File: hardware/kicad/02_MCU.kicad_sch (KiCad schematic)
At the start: 17 parts, among them SW1 RESET, SW2 BOOT, U3 ESP32-S3-MINI-1-N8

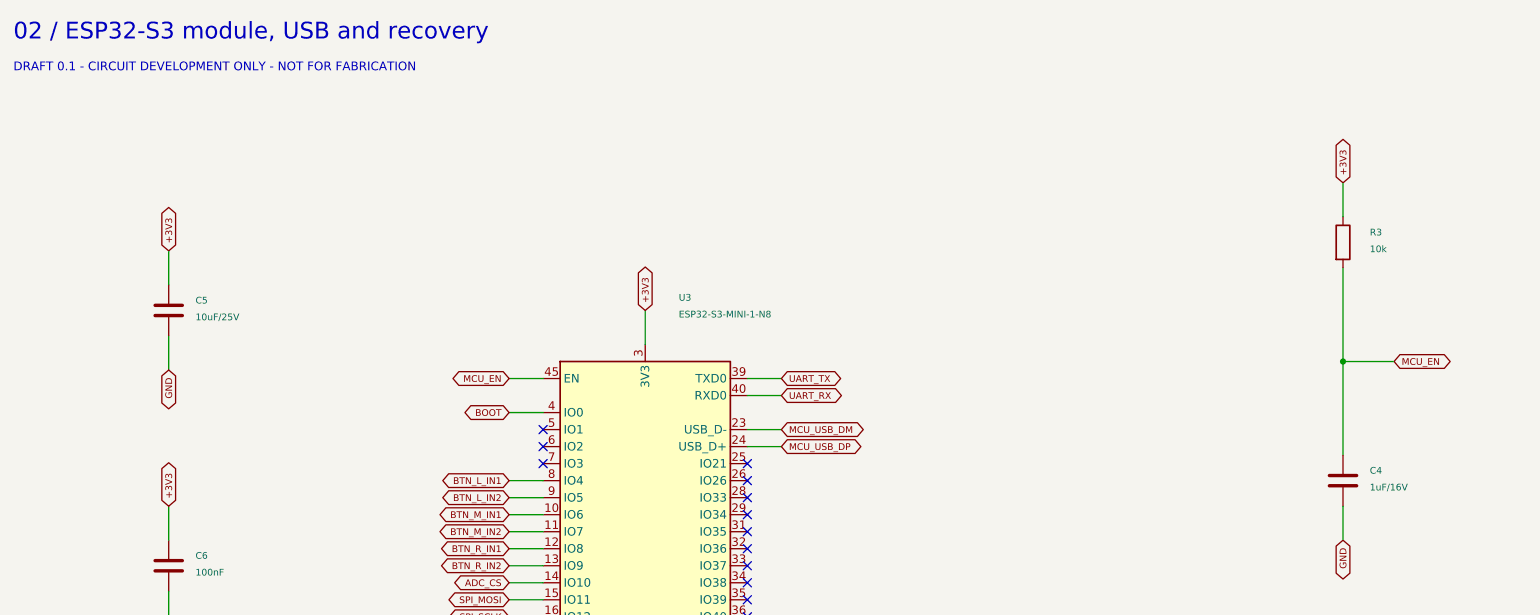
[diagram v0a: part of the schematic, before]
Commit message: Resolve KiCad component sourcing and missing footprints
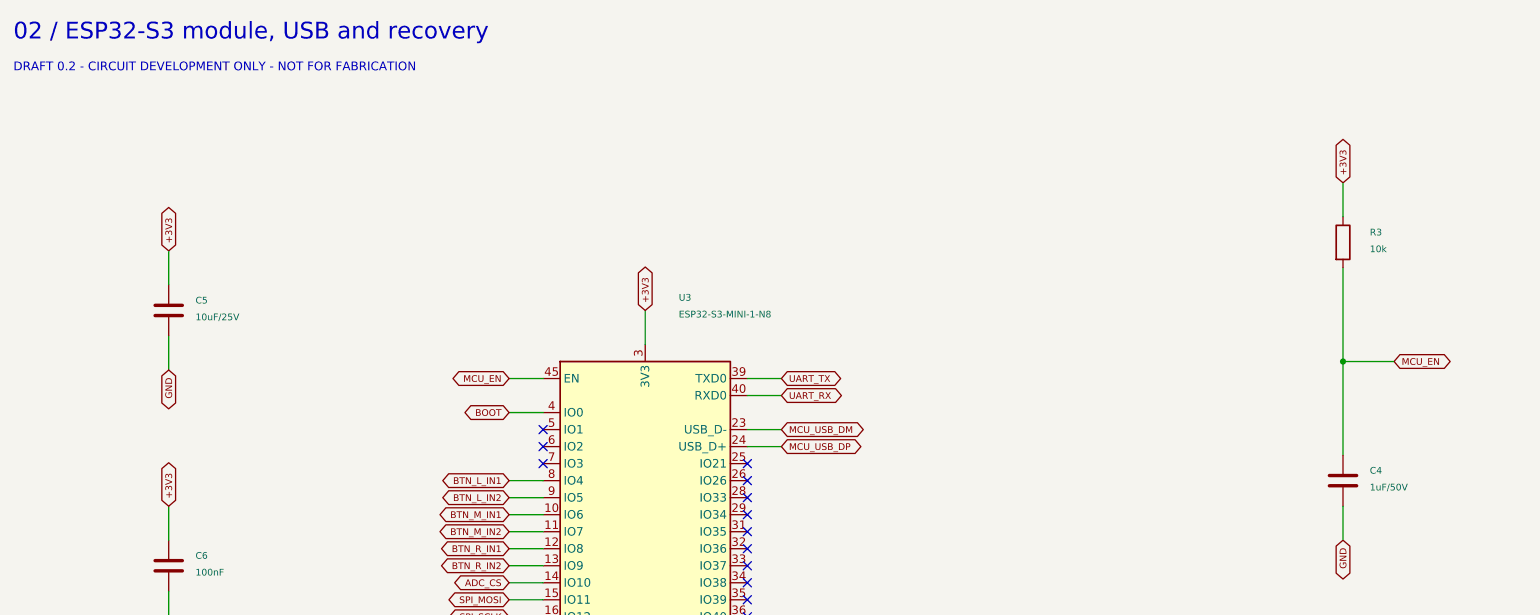
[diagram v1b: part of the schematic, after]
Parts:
- C4: value 1uF/16V -> 1uF/50V; Checked (none) -> 2026-09-08; JLCPCB Library Type (none) -> Basic; JLCPCB Part # (none) -> C15849; LCSC (none) -> C15849; MPN (none) -> CL10A105KB8NNNC; Manufacturer (none) -> Samsung Electro-Mechanics; Sourcing Status TBD - not orderable -> JLCPCB catalog verified; stock/quote refresh required; Supplier URL (none) -> https://jlcpcb.com/partdetail/16531-CL10A105KB8NNNC/C15849
- SW1, SW2: footprint (none) -> Button_Switch_SMD:SW_SPST_TS-1088-xR020; Checked (none) -> 2026-09-08; JLCPCB Library Type (none) -> Basic; JLCPCB Part # (none) -> C720477; LCSC (none) -> C720477; MPN (none) -> TS-1088-AR02016; Manufacturer (none) -> XUNPU; Sourcing Status TBD - select JLC tactile switch and footprint -> JLCPCB catalog verified; stock/quote refresh required; Supplier URL (none) -> https://jlcpcb.com/partdetail/XUNPU-TS_1088AR02016/C720477
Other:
- note added: "DRAFT 0.2 - CIRCUIT DEVELOPMENT ONLY - NOT FOR FABRICATION"
- note removed: "DRAFT 0.1 - CIRCUIT DEVELOPMENT ONLY - NOT FOR FABRICATION"
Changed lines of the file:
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@@
     (title "MagMouse - 02_MCU")
     (date "2026-09-08")
-    (rev "0.1 DRAFT")
+    (rev "0.2 DRAFT")
     (company "MagMouse")
     (comment 1 "NOT FOR FABRICATION - unresolved circuits listed in README.md"))
@@
       (justify left top))
 )
-  (text "DRAFT 0.1 - CIRCUIT DEVELOPMENT ONLY - NOT FOR FABRICATION"
+  (text "DRAFT 0.2 - CIRCUIT DEVELOPMENT ONLY - NOT FOR FABRICATION"
     (at 20 24 0)
     (effects
@@
           (size 1.0 1.0))
         (justify left)))
-    (property "Value" "1uF/16V"
+    (property "Value" "1uF/50V"
       (at 222.44 87.36 0)
       (effects
@@
           (size 1.0 1.0))
         (justify left)))
-    (property "Manufacturer" ""
+    (property "Manufacturer" "Samsung Electro-Mechanics"
       (at 218.44 86.36 0)
       (hide yes)
@@
           (size 1.0 1.0))
         (justify left)))
-    (property "MPN" ""
+    (property "MPN" "CL10A105KB8NNNC"
       (at 218.44 86.36 0)
       (hide yes)
@@
           (size 1.0 1.0))
         (justify left)))
-    (property "LCSC" ""
+    (property "LCSC" "C15849"
       (at 218.44 86.36 0)
       (hide yes)
@@
           (size 1.0 1.0))
         (justify left)))
-    (property "JLCPCB Part #" ""
+    (property "JLCPCB Part #" "C15849"
       (at 218.44 86.36 0)
       (hide yes)
@@
           (size 1.0 1.0))
         (justify left)))
-    (property "Sourcing Status" "TBD - not orderable"
+    (property "Sourcing Status" "JLCPCB catalog verified; stock/quote refresh required"
       (at 218.44 86.36 0)
       (hide yes)
@@
           (size 1.0 1.0))
         (justify left)))
-    (property "Checked" ""
+    (property "Checked" "2026-09-08"
       (at 218.44 86.36 0)
       (hide yes)
@@
         (path "/5d73110b-42e6-5c5c-9841-c82d60f67640/d5629ffc-c70c-5a32-8660-d50043bd3c4c"
           (reference "C4")
-          (unit 1)))))
+          (unit 1))))
+    (property "Supplier URL" "https://jlcpcb.com/partdetail/16531-CL10A105KB8NNNC/C15849"
+      (at 218.44 86.36 0)
+      (hide yes)
+      (effects
+        (font
+          (size 1 1))
+        (justify left)))
+    (property "JLCPCB Library Type" "Basic"
+      (at 218.44 86.36 0)
+      (hide yes)
+      (effects
+        (font
+          (size 1 1))
+        (justify left))))
   (wire
     (pts
@@
           (size 1.0 1.0))
         (justify left)))
-    (property "Footprint" ""
+    (property "Footprint" "Button_Switch_SMD:SW_SPST_TS-1088-xR020"
       (at 218.44 121.92 0)
       (hide yes)
@@
           (size 1.0 1.0))
         (justify left)))
-    (property "Datasheet" ""
+    (property "Datasheet" "https://datasheet.lcsc.com/datasheet/pdf/0475ac02febf455ca9ddcfb380b0df0d.pdf?productCode=C720477"
       (at 218.44 121.92 0)
       (hide yes)
@@
           (size 1.0 1.0))
         (justify left)))
-    (property "Manufacturer" ""
+    (property "Manufacturer" "XUNPU"
       (at 218.44 121.92 0)
       (hide yes)
@@
           (size 1.0 1.0))
         (justify left)))
-    (property "MPN" ""
+    (property "MPN" "TS-1088-AR02016"
       (at 218.44 121.92 0)
       (hide yes)
@@
           (size 1.0 1.0))
         (justify left)))
-    (property "LCSC" ""
+    (property "LCSC" "C720477"
       (at 218.44 121.92 0)
       (hide yes)
@@
           (size 1.0 1.0))
         (justify left)))
-    (property "JLCPCB Part #" ""
+    (property "JLCPCB Part #" "C720477"
       (at 218.44 121.92 0)
       (hide yes)
@@
           (size 1.0 1.0))
         (justify left)))
-    (property "Sourcing Status" "TBD - select JLC tactile switch and footprint"
+    (property "Sourcing Status" "JLCPCB catalog verified; stock/quote refresh required"
       (at 218.44 121.92 0)
       (hide yes)
@@
           (size 1.0 1.0))
         (justify left)))
-    (property "Checked" ""
+    (property "Checked" "2026-09-08"
       (at 218.44 121.92 0)
       (hide yes)
@@
         (path "/5d73110b-42e6-5c5c-9841-c82d60f67640/d5629ffc-c70c-5a32-8660-d50043bd3c4c"
           (reference "SW1")
-          (unit 1)))))
+          (unit 1))))
+    (property "Supplier URL" "https://jlcpcb.com/partdetail/XUNPU-TS_1088AR02016/C720477"
+      (at 218.44 121.92 0)
+      (hide yes)
+      (effects
+        (font
+          (size 1 1))
+        (justify left)))
+    (property "JLCPCB Library Type" "Basic"
+      (at 218.44 121.92 0)
+      (hide yes)
+      (effects
+        (font
+          (size 1 1))
+        (justify left))))
   (wire
     (pts
@@
           (size 1.0 1.0))
         (justify left)))
-    (property "Footprint" ""
+    (property "Footprint" "Button_Switch_SMD:SW_SPST_TS-1088-xR020"
       (at 289.56 121.92 0)
       (hide yes)
@@
           (size 1.0 1.0))
         (justify left)))
-    (property "Datasheet" ""
+    (property "Datasheet" "https://datasheet.lcsc.com/datasheet/pdf/0475ac02febf455ca9ddcfb380b0df0d.pdf?productCode=C720477"
       (at 289.56 121.92 0)
       (hide yes)
@@
           (size 1.0 1.0))
         (justify left)))
-    (property "Manufacturer" ""
+    (property "Manufacturer" "XUNPU"
       (at 289.56 121.92 0)
       (hide yes)
@@
           (size 1.0 1.0))
         (justify left)))
-    (property "MPN" ""
+    (property "MPN" "TS-1088-AR02016"
       (at 289.56 121.92 0)
       (hide yes)
@@
           (size 1.0 1.0))
         (justify left)))
-    (property "LCSC" ""
+    (property "LCSC" "C720477"
       (at 289.56 121.92 0)
       (hide yes)
@@
           (size 1.0 1.0))
         (justify left)))
-    (property "JLCPCB Part #" ""
+    (property "JLCPCB Part #" "C720477"
       (at 289.56 121.92 0)
       (hide yes)
@@
           (size 1.0 1.0))
         (justify left)))
-    (property "Sourcing Status" "TBD - select JLC tactile switch and footprint"
+    (property "Sourcing Status" "JLCPCB catalog verified; stock/quote refresh required"
       (at 289.56 121.92 0)
       (hide yes)
@@
           (size 1.0 1.0))
         (justify left)))
-    (property "Checked" ""
+    (property "Checked" "2026-09-08"
       (at 289.56 121.92 0)
       (hide yes)
@@
         (path "/5d73110b-42e6-5c5c-9841-c82d60f67640/d5629ffc-c70c-5a32-8660-d50043bd3c4c"
           (reference "SW2")
-          (unit 1)))))
-  (wire
-    (pts
+          (unit 1))))
+    (property "Supplier URL" "https://jlcpcb.com/partdetail/XUNPU-TS_1088AR02016/C720477"
+      (at 289.56 121.92 0)
+      (hide yes)
+      (effects
+        (font
+          (size 1 1))
+        (justify left)))
+    (property "JLCPCB Library Type" "Basic"
+      (at 289.56 121.92 0)
+      (hide yes)
+      (effects
+        (font
+          (size 1 1))
+        (justify left))))
+  (wire
+    (pts

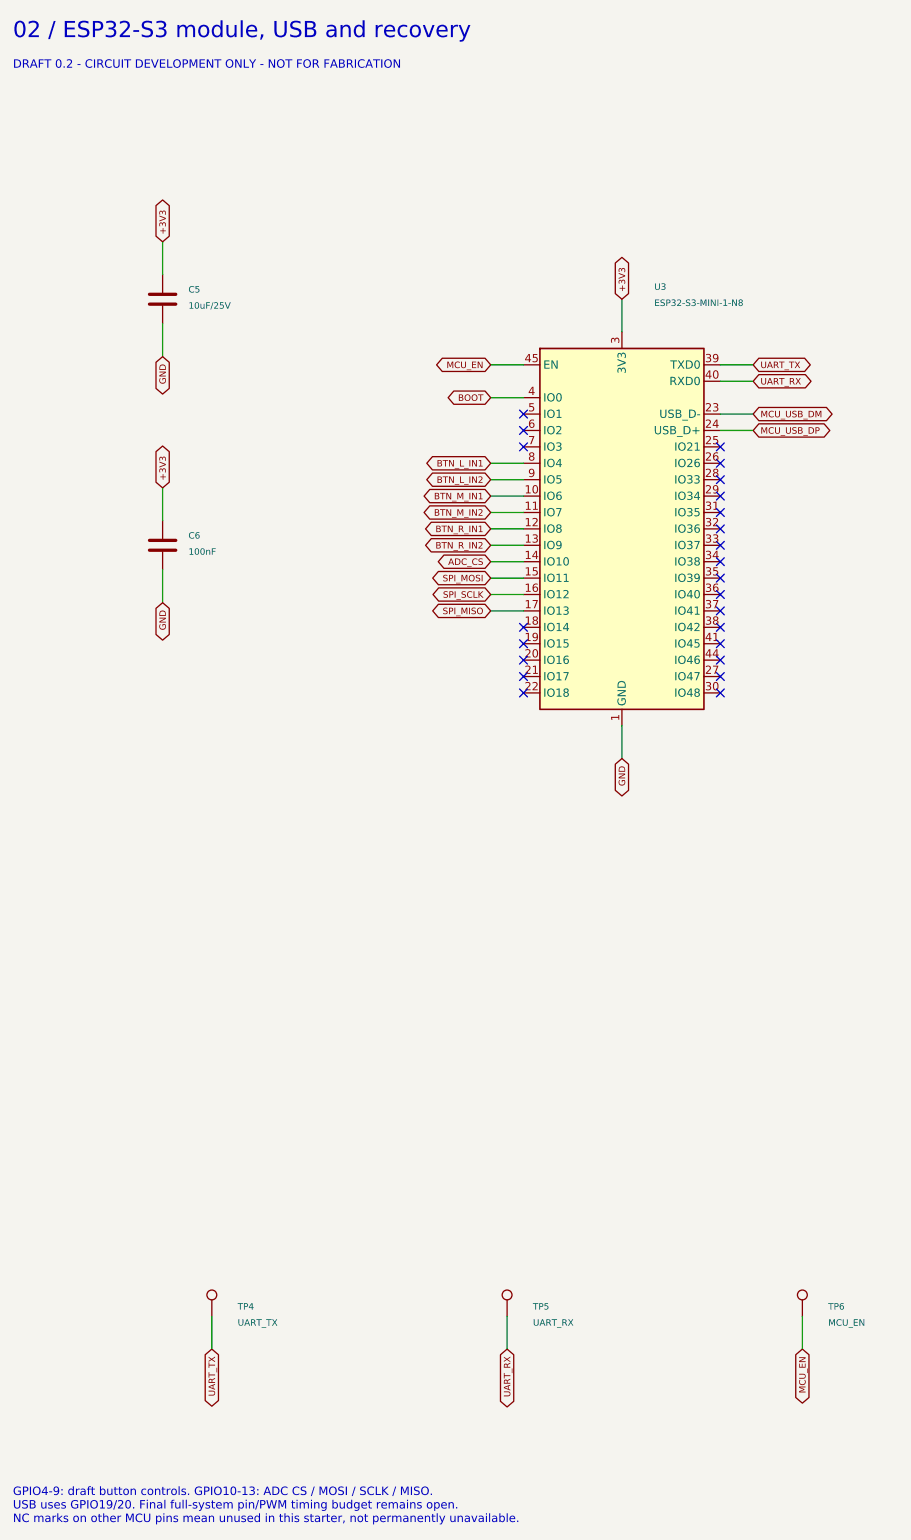
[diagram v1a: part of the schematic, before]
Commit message: Implement USB-C power control schematic and validation
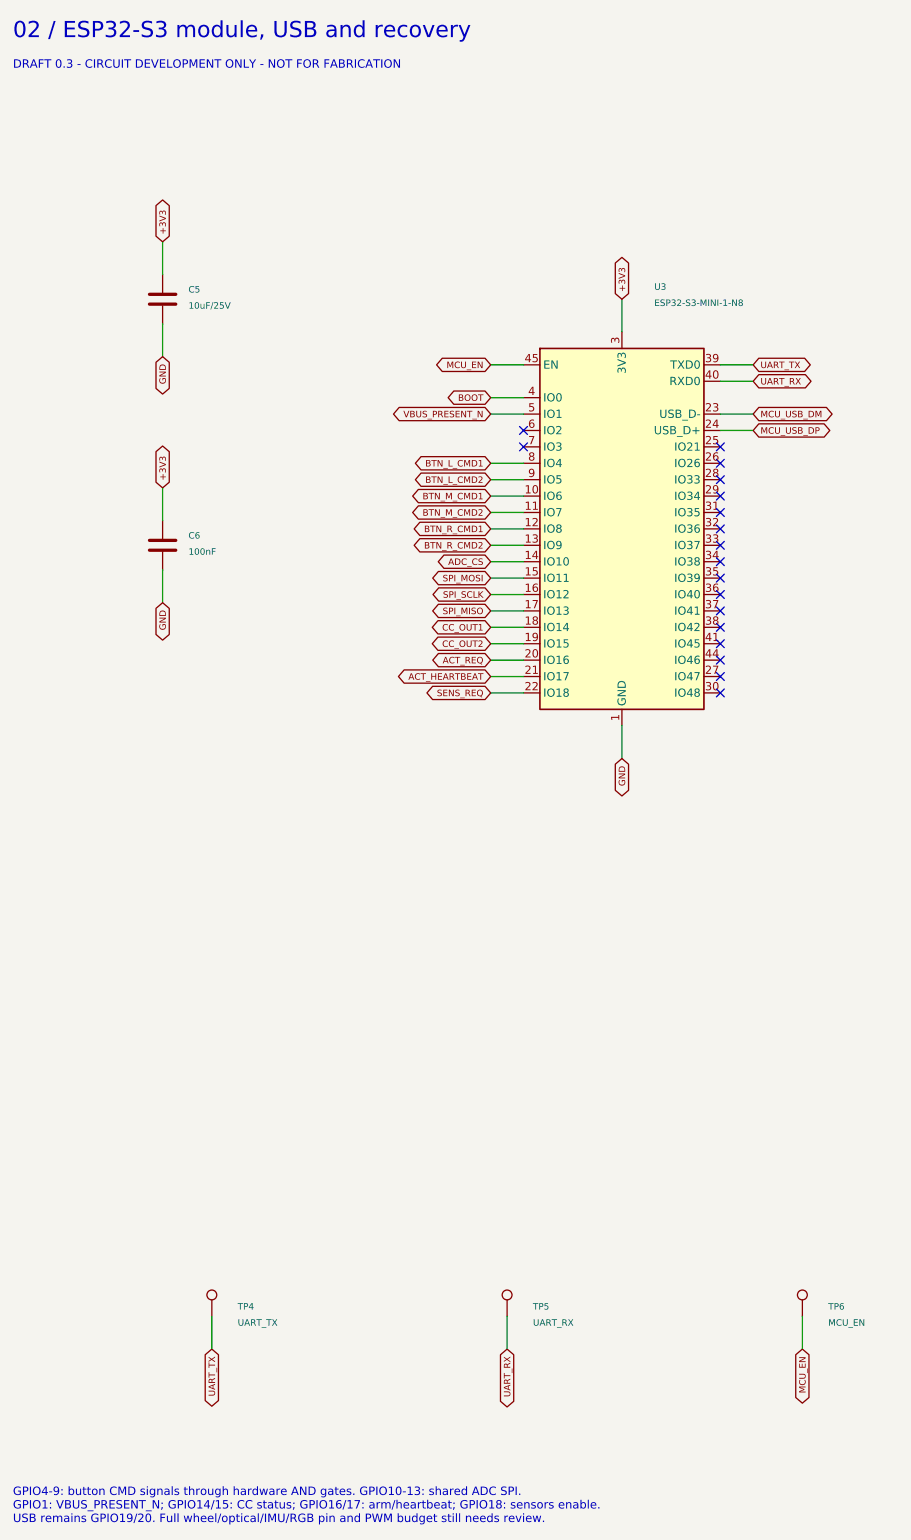
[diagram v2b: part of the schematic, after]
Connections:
- net CC_OUT1: now reaches U3.18 (IO14)
- net CC_OUT2: now reaches U3.19 (IO15)
- net ACT_REQ: now reaches U3.20 (IO16)
- net ACT_HEARTBEAT: now reaches U3.21 (IO17)
- net SENS_REQ: now reaches U3.22 (IO18)
- net VBUS_PRESENT_N: now reaches U3.5 (IO1)
- net BTN_L_IN1 renamed BTN_L_CMD1
- net BTN_L_IN2 renamed BTN_L_CMD2
- net BTN_M_IN1 renamed BTN_M_CMD1
- net BTN_M_IN2 renamed BTN_M_CMD2
- net BTN_R_IN1 renamed BTN_R_CMD1
- net BTN_R_IN2 renamed BTN_R_CMD2
- no-connect marks 24 -> 18
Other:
- note added: "DRAFT 0.3 - CIRCUIT DEVELOPMENT ONLY - NOT FOR FABRICATION"
- note added: "GPIO4-9: button CMD signals through hardware AND gates. GPIO10-13: shared ADC SPI. GPIO1: VBUS_PRESENT_N; GPIO14/15: CC status; GPIO16/17: arm/heartbeat; GPIO18: sensors enable. USB remains GPIO19/20. Full wheel/optical/IMU/RGB pin and PWM budget still needs review."
- note removed: "DRAFT 0.2 - CIRCUIT DEVELOPMENT ONLY - NOT FOR FABRICATION"
- note removed: "GPIO4-9: draft button controls. GPIO10-13: ADC CS / MOSI / SCLK / MISO. USB uses GPIO19/20. Final full-system pin/PWM timing budget remains open. NC marks on other MCU pins mean unused in this starter, not permanently unavailable."
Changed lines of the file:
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@@
     (title "MagMouse - 02_MCU")
     (date "2026-09-08")
-    (rev "0.2 DRAFT")
+    (rev "0.3 DRAFT")
     (company "MagMouse")
     (comment 1 "NOT FOR FABRICATION - unresolved circuits listed in README.md"))
@@
       (justify left top))
 )
-  (text "DRAFT 0.2 - CIRCUIT DEVELOPMENT ONLY - NOT FOR FABRICATION"
+  (text "DRAFT 0.3 - CIRCUIT DEVELOPMENT ONLY - NOT FOR FABRICATION"
     (at 20 24 0)
     (effects
@@
 )
   (no_connect
-    (at 99.06 78.74)
-)
-  (no_connect
     (at 99.06 81.28)
 )
@@
       (type default))
 )
-  (global_label "BTN_L_IN1"
+  (global_label "BTN_L_CMD1"
     (shape bidirectional)
     (at 93.98 86.36 180)
@@
       (type default))
 )
-  (global_label "BTN_L_IN2"
+  (global_label "BTN_L_CMD2"
     (shape bidirectional)
     (at 93.98 88.9 180)
@@
       (type default))
 )
-  (global_label "BTN_M_IN1"
+  (global_label "BTN_M_CMD1"
     (shape bidirectional)
     (at 93.98 91.44 180)
@@
       (type default))
 )
-  (global_label "BTN_M_IN2"
+  (global_label "BTN_M_CMD2"
     (shape bidirectional)
     (at 93.98 93.98 180)
@@
       (type default))
 )
-  (global_label "BTN_R_IN1"
+  (global_label "BTN_R_CMD1"
     (shape bidirectional)
     (at 93.98 96.52 180)
@@
       (type default))
 )
-  (global_label "BTN_R_IN2"
+  (global_label "BTN_R_CMD2"
     (shape bidirectional)
     (at 93.98 99.06 180)
@@
         (size 1.0 1.0))
       (justify right))
-)
-  (no_connect
-    (at 99.06 111.76)
-)
-  (no_connect
-    (at 99.06 114.3)
-)
-  (no_connect
-    (at 99.06 116.84)
-)
-  (no_connect
-    (at 99.06 119.38)
-)
-  (no_connect
-    (at 99.06 121.92)
 )
   (wire
@@
       (justify right))
 )
-  (text "GPIO4-9: draft button controls. GPIO10-13: ADC CS / MOSI / SCLK / MISO.\nUSB uses GPIO19/20. Final full-system pin/PWM timing budget remains open.\nNC marks on other MCU pins mean unused in this starter, not permanently unavailable."
+  (text "GPIO4-9: button CMD signals through hardware AND gates. GPIO10-13: shared ADC SPI.\nGPIO1: VBUS_PRESENT_N; GPIO14/15: CC status; GPIO16/17: arm/heartbeat; GPIO18: sensors enable.\nUSB remains GPIO19/20. Full wheel/optical/IMU/RGB pin and PWM budget still needs review."
     (at 20 245 0)
     (effects
@@
       (justify left top))
 )
-  (embedded_fonts no))
+  (embedded_fonts no)
+  (wire
+    (pts
+      (xy 99.06 78.74)
+      (xy 93.98 78.74))
+    (stroke
+      (width 0)
+      (type default))
+)
+  (global_label "VBUS_PRESENT_N"
+    (shape bidirectional)
+    (at 93.98 78.74 180)
+    (effects
+      (font
+        (size 1.0 1.0))
+      (justify right))
+)
+  (wire
+    (pts
+      (xy 99.06 111.75999999999999)
+      (xy 93.98 111.76))
+    (stroke
+      (width 0)
+      (type default))
+)
+  (global_label "CC_OUT1"
+    (shape bidirectional)
+    (at 93.98 111.76 180)
+    (effects
+      (font
+        (size 1.0 1.0))
+      (justify right))
+)
+  (wire
+    (pts
+      (xy 99.06 114.3)
+      (xy 93.98 114.3))
+    (stroke
+      (width 0)
+      (type default))
+)
+  (global_label "CC_OUT2"
+    (shape bidirectional)
+    (at 93.98 114.3 180)
+    (effects
+      (font
+        (size 1.0 1.0))
+      (justify right))
+)
+  (wire
+    (pts
+      (xy 99.06 116.84)
+      (xy 93.98 116.84))
+    (stroke
+      (width 0)
+      (type default))
+)
+  (global_label "ACT_REQ"
+    (shape bidirectional)
+    (at 93.98 116.84 180)
+    (effects
+      (font
+        (size 1.0 1.0))
+      (justify right))
+)
+  (wire
+    (pts
+      (xy 99.06 119.38)
+      (xy 93.98 119.38))
+    (stroke
+      (width 0)
+      (type default))
+)
+  (global_label "ACT_HEARTBEAT"
+    (shape bidirectional)
+    (at 93.98 119.38 180)
+    (effects
+      (font
+        (size 1.0 1.0))
+      (justify right))
+)
+  (wire
+    (pts
+      (xy 99.06 121.91999999999999)
+      (xy 93.98 121.92))
+    (stroke
+      (width 0)
+      (type default))
+)
+  (global_label "SENS_REQ"
+    (shape bidirectional)
+    (at 93.98 121.92 180)
+    (effects
+      (font
+        (size 1.0 1.0))
+      (justify right))
+))
